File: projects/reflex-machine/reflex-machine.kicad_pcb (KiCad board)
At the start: 2 copper layers, 160 x 125 mm, 125 parts, among them J1 12V_IN, J10 MAG9, J11 MAG10, J12 COIN, J13 BUTTONS, J14 STATUS_LEDS, J15 7SEG, J16 MEGA SPARE, J17 ESP32 SPARE, J2 MAG1, J3 MAG2, J4 MAG3, J5 MAG4, J6 MAG5, J7 MAG6, J8 MAG7, J9 MAG8, Q1 IRLZ44N, Q10 IRLZ44N, Q2 IRLZ44N, Q3 IRLZ44N, Q4 IRLZ44N, Q5 IRLZ44N, Q6 IRLZ44N, Q7 IRLZ44N, Q8 IRLZ44N, Q9 IRLZ44N, U1 5V 2A module (K7805-2000R3), U2 PC817, U3 74HC595N

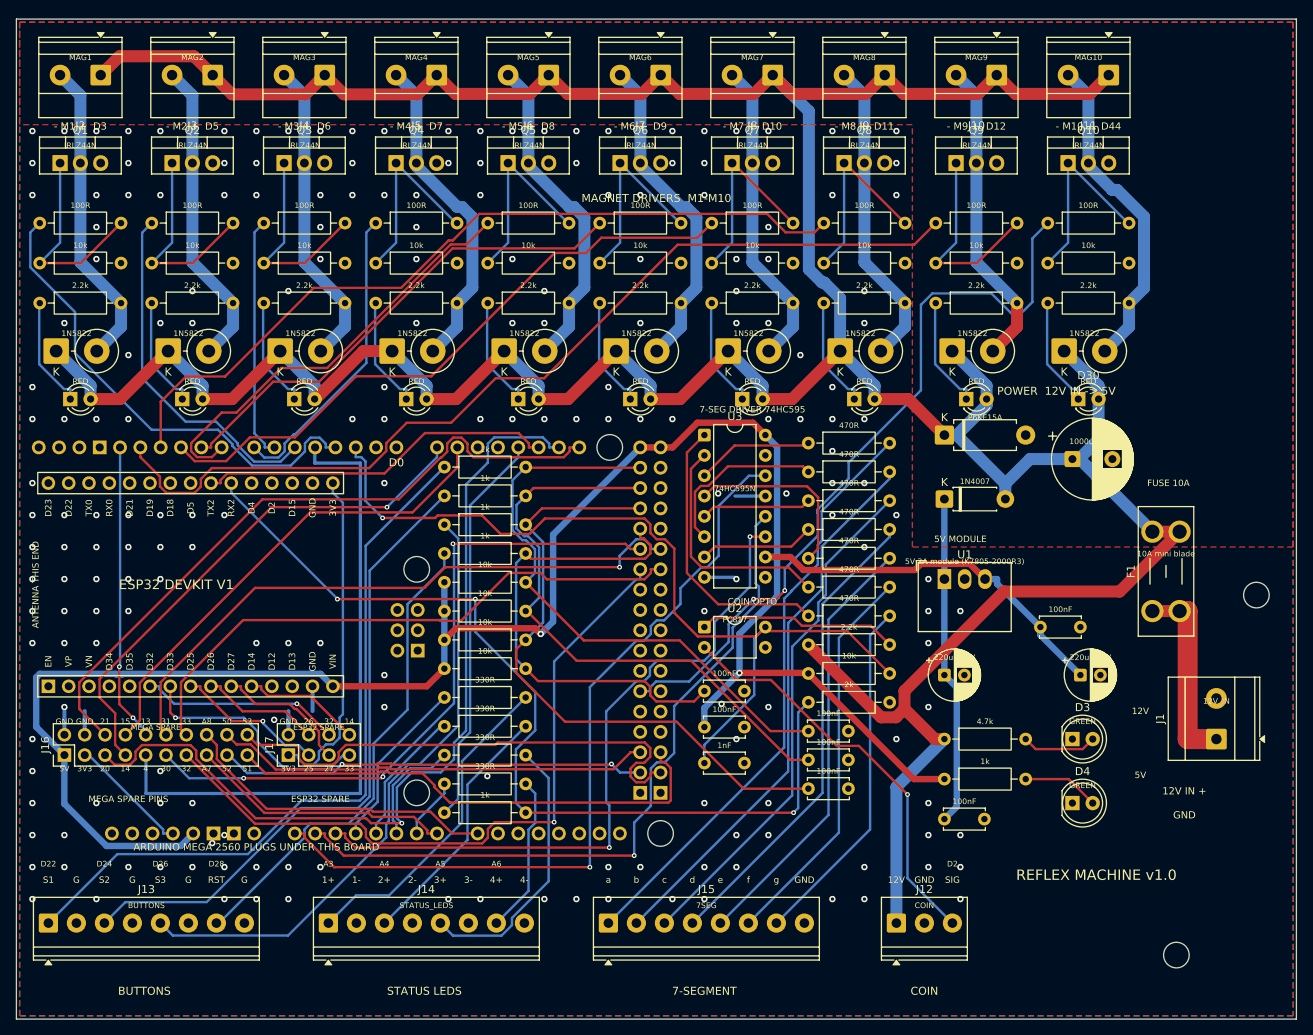
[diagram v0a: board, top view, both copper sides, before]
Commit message: fix(MD-T8): place decoupling caps at their IC supply pins (blinky C3, reflex C13)
Co-Authored-By: Claude Opus 5.5 <noreply@anthropic.com>
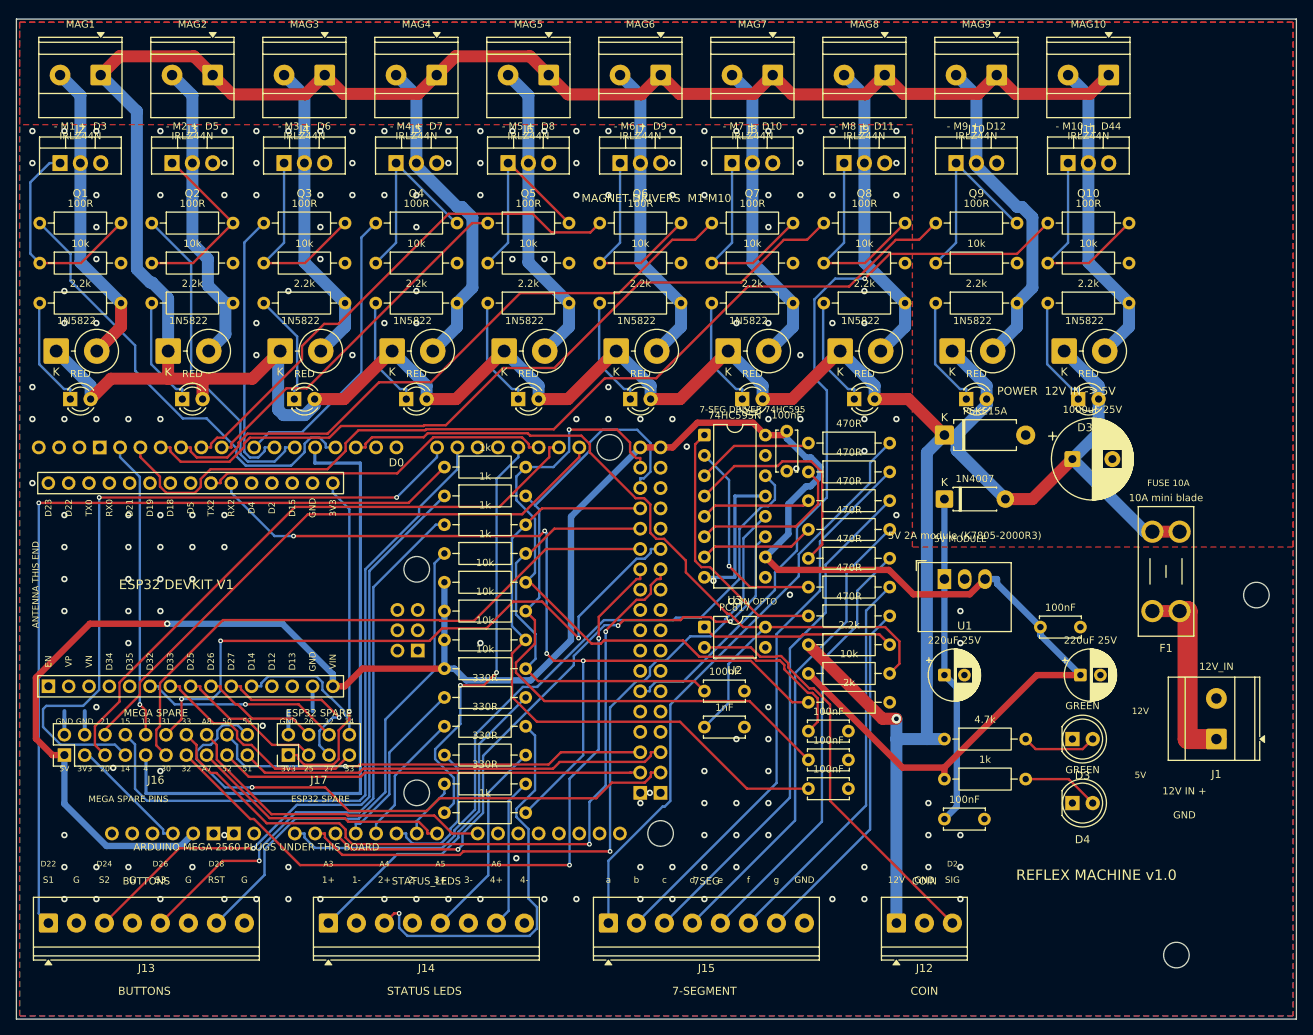
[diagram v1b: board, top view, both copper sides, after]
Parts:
- moved C13 38.4 mm to (196.3, 101.5), turned to -90 degrees
- moved C8 4.50 mm to (186.0, 138.5)
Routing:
- net /I2C_SDA: track 108.4 -> 78.7 mm, vias 1 -> 0
- net /SPARE_TX3: track 65.7 -> 91.6 mm, vias 1 -> 2
- net /SPARE_RX3: track 60.6 -> 85.2 mm
- net /SPARE_D33: track 73.6 -> 96.6 mm, vias 0 -> 2
- net /LED2_OUT: track 31.9 -> 49.9 mm, vias 0 -> 1
- net /BTN_S2: track 74.8 -> 92.1 mm
- net /BTN_S1_EXT: track 91.3 -> 105.6 mm, vias 0 -> 1
- net /BTN_S1: track 74.4 -> 85.3 mm, vias 0 -> 1
- net GND: track 19.6 -> 29.8 mm, vias 202 -> 172
- net /I2C_SCL: track 86.0 -> 76.2 mm
- net /LED3_OUT: track 34.5 -> 25.4 mm
- net /MAG5_PWM: track 54.1 -> 45.2 mm
- net /SPARE_MOSI: track 62.7 -> 53.9 mm
- net +5V: track 279.3 -> 287.5 mm, vias 2 -> 1
- net /SPARE_D30: track 84.9 -> 76.7 mm, vias 3 -> 0
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
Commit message: fix(MD-T10): reflex 12 V input path sized for 10 A
Co-Authored-By: Claude Opus 5.5 <noreply@anthropic.com>
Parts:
- moved C10 0.40 mm to (199.4, 142.6)
- moved C11 0.40 mm to (199.4, 146.2)
- moved C9 0.40 mm to (199.4, 139.0)
- moved R41 0.40 mm to (199.4, 128.2)
- moved R42 0.40 mm to (199.4, 131.8)
- moved R55 0.40 mm to (199.4, 103.0)
- moved R56 0.40 mm to (199.4, 106.6)
- moved R57 0.40 mm to (199.4, 110.2)
- moved R58 0.40 mm to (199.4, 113.8)
- moved R59 0.40 mm to (199.4, 117.4)
- moved R60 0.40 mm to (199.4, 121.0)
- moved R61 0.40 mm to (199.4, 124.6)
- moved R63 0.40 mm to (199.4, 135.4)
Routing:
- net +5V: track 287.5 -> 259.0 mm, vias 1 -> 0
- net /I2C_SCL: track 76.2 -> 103.3 mm
- net /I2C_SDA: track 78.7 -> 104.4 mm, vias 0 -> 1
- net /ESP_TX2: track 44.3 -> 63.7 mm
- net /SPARE_RX3: track 85.2 -> 66.2 mm
- net /LED2_OUT: track 49.9 -> 31.9 mm, vias 1 -> 0
- net /SPARE_D32: track 94.5 -> 77.8 mm, vias 2 -> 1
- net /BTN_S2: track 92.1 -> 75.5 mm
- net /SPARE_D33: track 96.6 -> 80.9 mm, vias 2 -> 0
- net /ESP_RX2: track 115.5 -> 127.7 mm, vias 4 -> 5
- net /ESP_IO32: track 25.1 -> 36.3 mm, vias 1 -> 0
- net /SPARE_CS: track 72.7 -> 61.9 mm, vias 1 -> 0
- net /SEG_QC: track 26.1 -> 36.6 mm, vias 1 -> 0
- net /SPARE_TX3: track 91.6 -> 81.3 mm, vias 2 -> 0
- net GND: track 29.8 -> 19.6 mm, vias 172 -> 179
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- added copper zone on F.Cu, net /+12V_IN

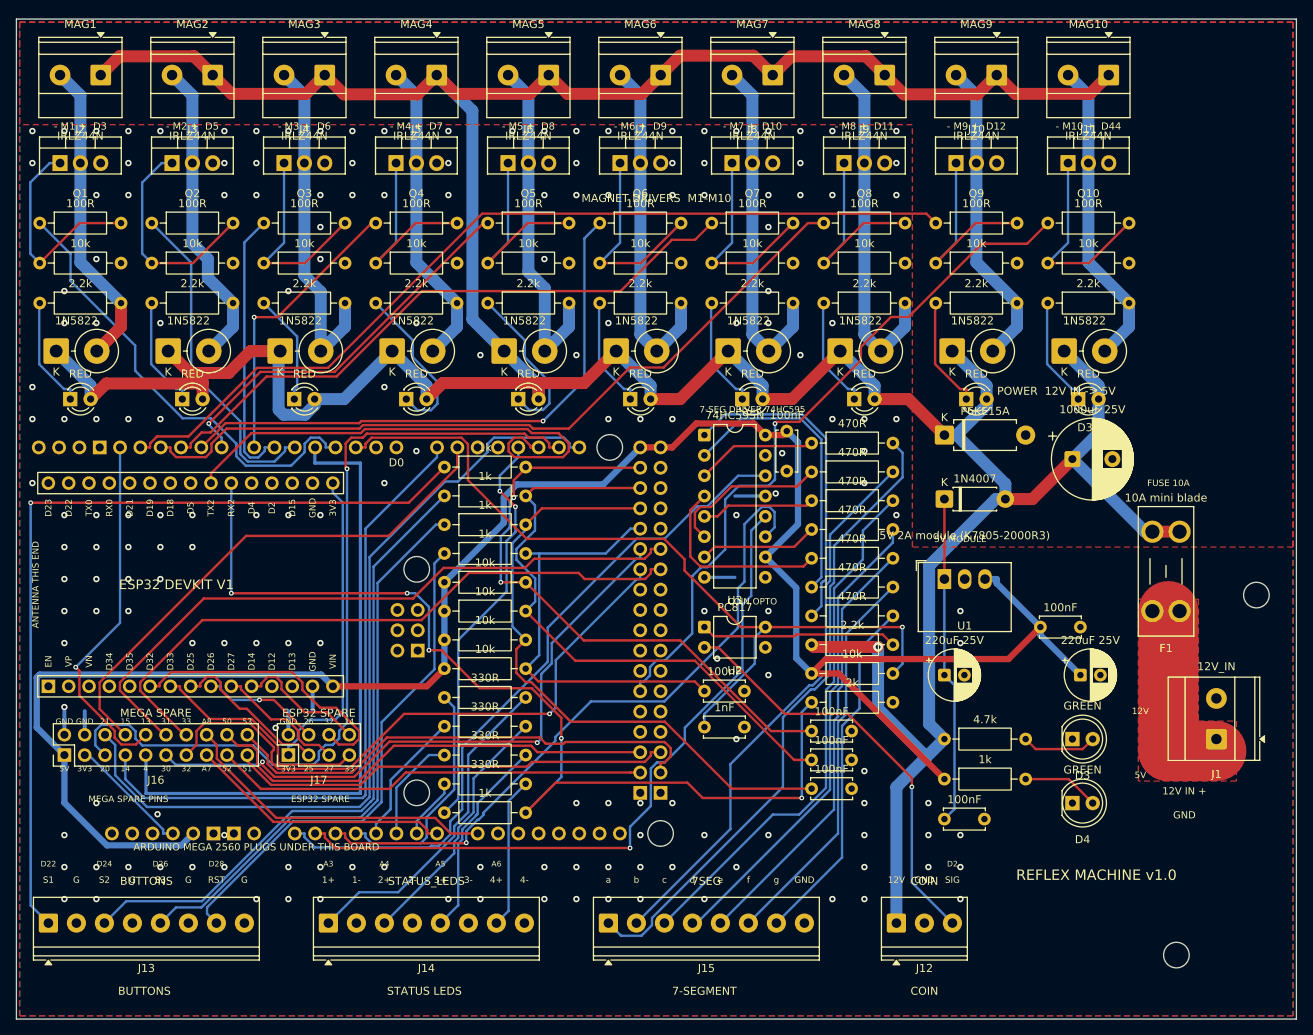
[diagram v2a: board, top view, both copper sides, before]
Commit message: fix(MD-T11): derive via/stitch spacing from fab rules (no flaky hole_to_hole)
Co-Authored-By: Claude Opus 5.5 <noreply@anthropic.com>
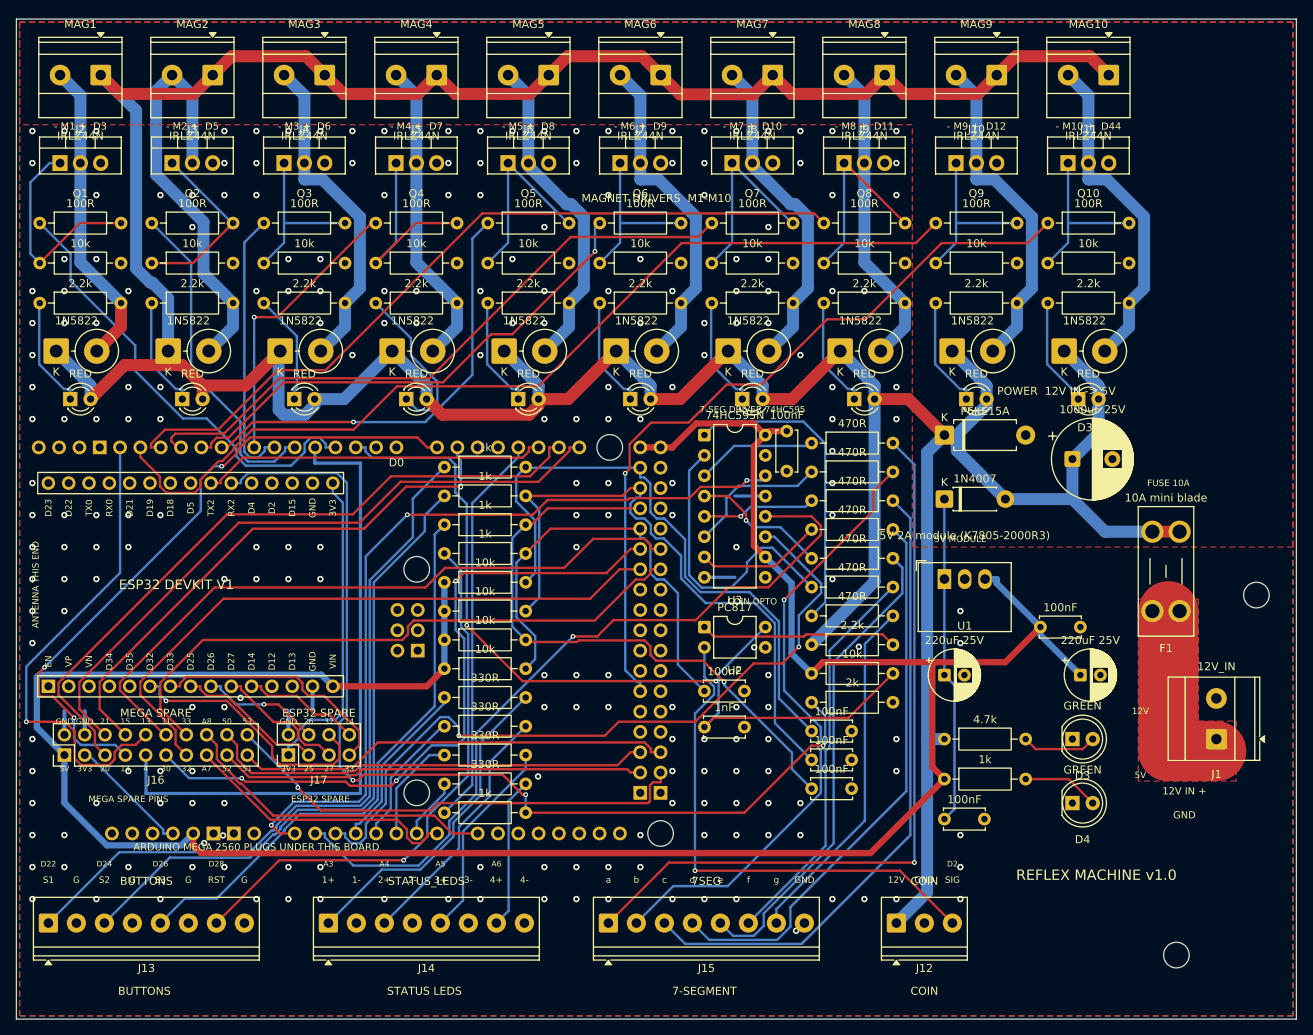
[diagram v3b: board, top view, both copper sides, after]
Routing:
- net +5V: track 259.0 -> 316.8 mm
- net /I2C_SCL: track 103.3 -> 82.8 mm
- net /ESP_TX2: track 63.7 -> 43.3 mm
- net /I2C_SDA: track 104.4 -> 86.9 mm, vias 1 -> 0
- net /BTN_S1_EXT: track 107.0 -> 91.9 mm, vias 1 -> 0
- net /SPARE_D13: track 45.3 -> 60.4 mm
- net /SEG_A: track 80.7 -> 94.9 mm, vias 0 -> 1
- net /MAG2_OUT: track 38.9 -> 52.6 mm
- net /SEG_DATA: track 87.1 -> 100.7 mm, vias 0 -> 3
- net /SEG_C: track 66.6 -> 80.2 mm
- net +12V: track 507.2 -> 519.6 mm, vias 1 -> 0
- net /COIN_SIG: track 52.9 -> 64.3 mm
- net /SEG_D: track 59.9 -> 70.2 mm
- net /MAG6_PWM: track 71.8 -> 63.4 mm
- net /SEG_CLOCK: track 85.4 -> 93.3 mm, vias 1 -> 2
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
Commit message: wip(MD-T12): +12V_IN as 2.5 mm skeleton during routing, 10 A pour after routing - saved before handover
Co-Authored-By: Claude Opus 5.5 <noreply@anthropic.com>
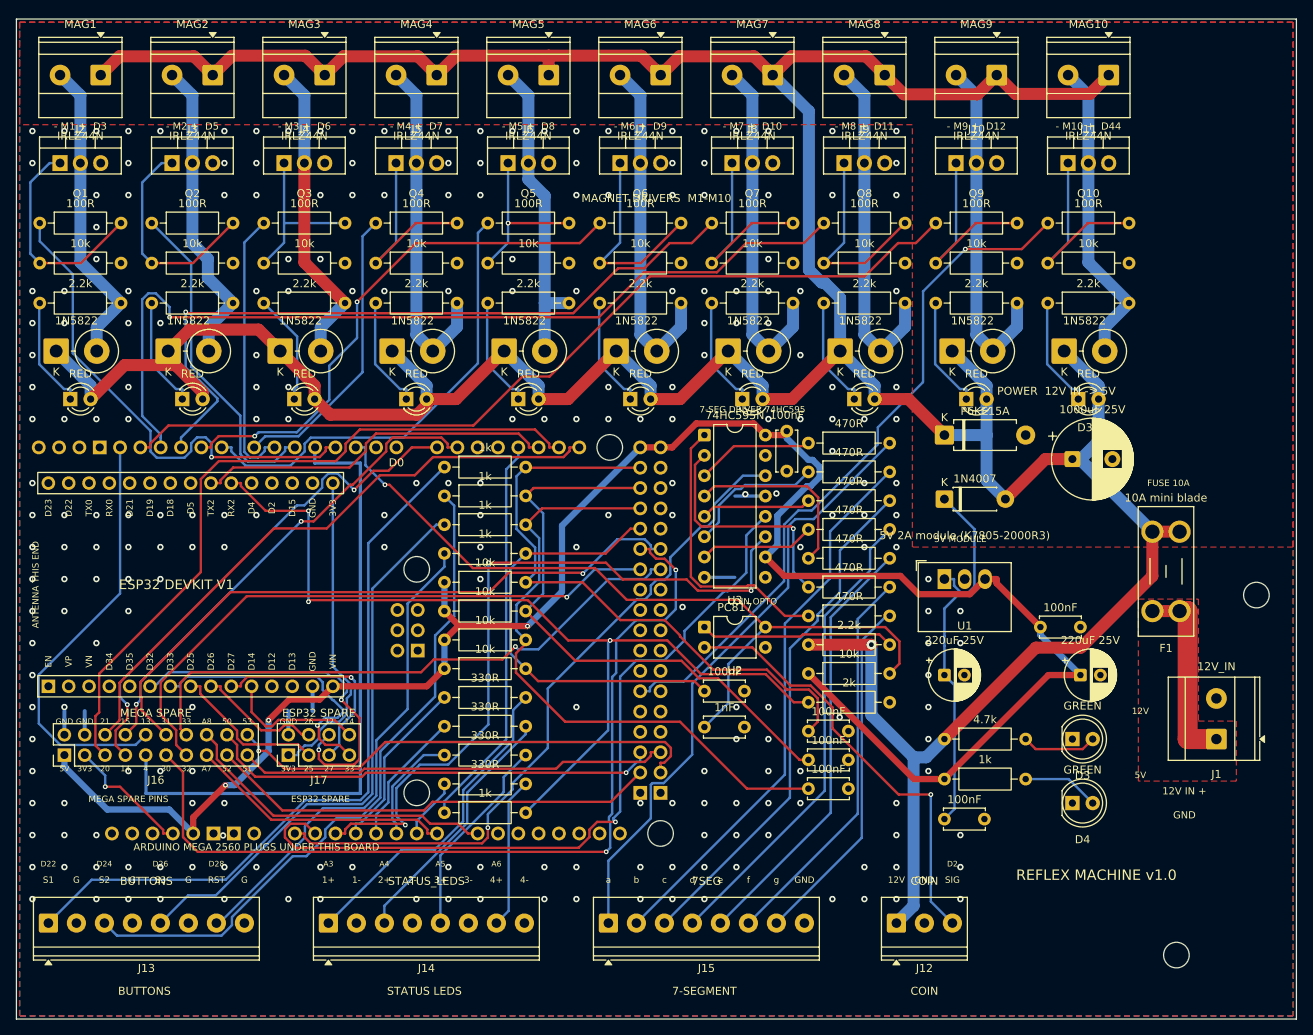
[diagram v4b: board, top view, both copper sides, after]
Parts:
- moved C10 0.40 mm to (199.0, 142.6)
- moved C11 0.40 mm to (199.0, 146.2)
- moved C9 0.40 mm to (199.0, 139.0)
- moved R41 0.40 mm to (199.0, 128.2)
- moved R42 0.40 mm to (199.0, 131.8)
- moved R55 0.40 mm to (199.0, 103.0)
- moved R56 0.40 mm to (199.0, 106.6)
- moved R57 0.40 mm to (199.0, 110.2)
- moved R58 0.40 mm to (199.0, 113.8)
- moved R59 0.40 mm to (199.0, 117.4)
- moved R60 0.40 mm to (199.0, 121.0)
- moved R61 0.40 mm to (199.0, 124.6)
- moved R63 0.40 mm to (199.0, 135.4)
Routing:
- net +5V: track 316.8 -> 247.5 mm, vias 0 -> 3
- net /SPARE_D30: track 86.2 -> 111.7 mm, vias 3 -> 2
- net /SPARE_TX3: track 83.1 -> 64.7 mm, vias 3 -> 2
- net /SEG_A: track 94.9 -> 76.7 mm, vias 1 -> 0
- net /SEG_C: track 80.2 -> 64.5 mm
- net /MAG2_OUT: track 52.6 -> 38.9 mm
- net /MAG8_PWM: track 98.2 -> 111.8 mm, vias 0 -> 1
- net /ESP_IO32: track 32.9 -> 45.6 mm, vias 1 -> 2
- net /SEG_DATA: track 100.7 -> 88.1 mm, vias 3 -> 1
- net /COIN_IN: track 110.6 -> 99.5 mm, vias 2 -> 1
- net /SEG_D: track 70.2 -> 59.4 mm
- net /ESP_IO27: track 16.6 -> 27.0 mm, vias 0 -> 1
- net /MAG7_PWM: track 80.6 -> 91.0 mm, vias 0 -> 1
- net +12V: track 519.6 -> 509.2 mm, vias 0 -> 1
- net /COIN_SIG: track 64.3 -> 54.6 mm
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
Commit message: fix(MD-T12): reflex routes reliably - 10 A path poured after routing; seeded retry
Co-Authored-By: Claude Opus 5.5 <noreply@anthropic.com>
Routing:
- net +5V: track 247.5 -> 277.9 mm, vias 3 -> 0
- net /SPARE_TX3: track 64.7 -> 83.4 mm, vias 2 -> 1
- net /MEGA_TX1: track 49.5 -> 66.6 mm, vias 0 -> 1
- net /BTN_S1_EXT: track 91.3 -> 107.5 mm, vias 0 -> 1
- net /SPARE_D13: track 53.7 -> 37.8 mm, vias 0 -> 1
- net /SPARE_D30: track 111.7 -> 96.9 mm, vias 2 -> 3
- net /MAG8_PWM: track 111.8 -> 97.2 mm, vias 1 -> 0
- net /MAG10_PWM: track 87.5 -> 101.0 mm
- net /SEG_B: track 69.5 -> 82.2 mm
- net /SPARE_D33: track 73.2 -> 84.4 mm
- net /MAG7_PWM: track 91.0 -> 80.2 mm
- net /SEG_CLOCK: track 91.5 -> 80.9 mm, vias 3 -> 1
- net /SPARE_MISO: track 56.8 -> 67.1 mm
- net /ESP_IO27: track 27.0 -> 17.0 mm, vias 1 -> 0
- net /ESP_IO32: track 45.6 -> 35.8 mm, vias 2 -> 0
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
